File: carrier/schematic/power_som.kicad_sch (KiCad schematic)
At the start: 17 parts, among them U22004 TPS54302DDCR

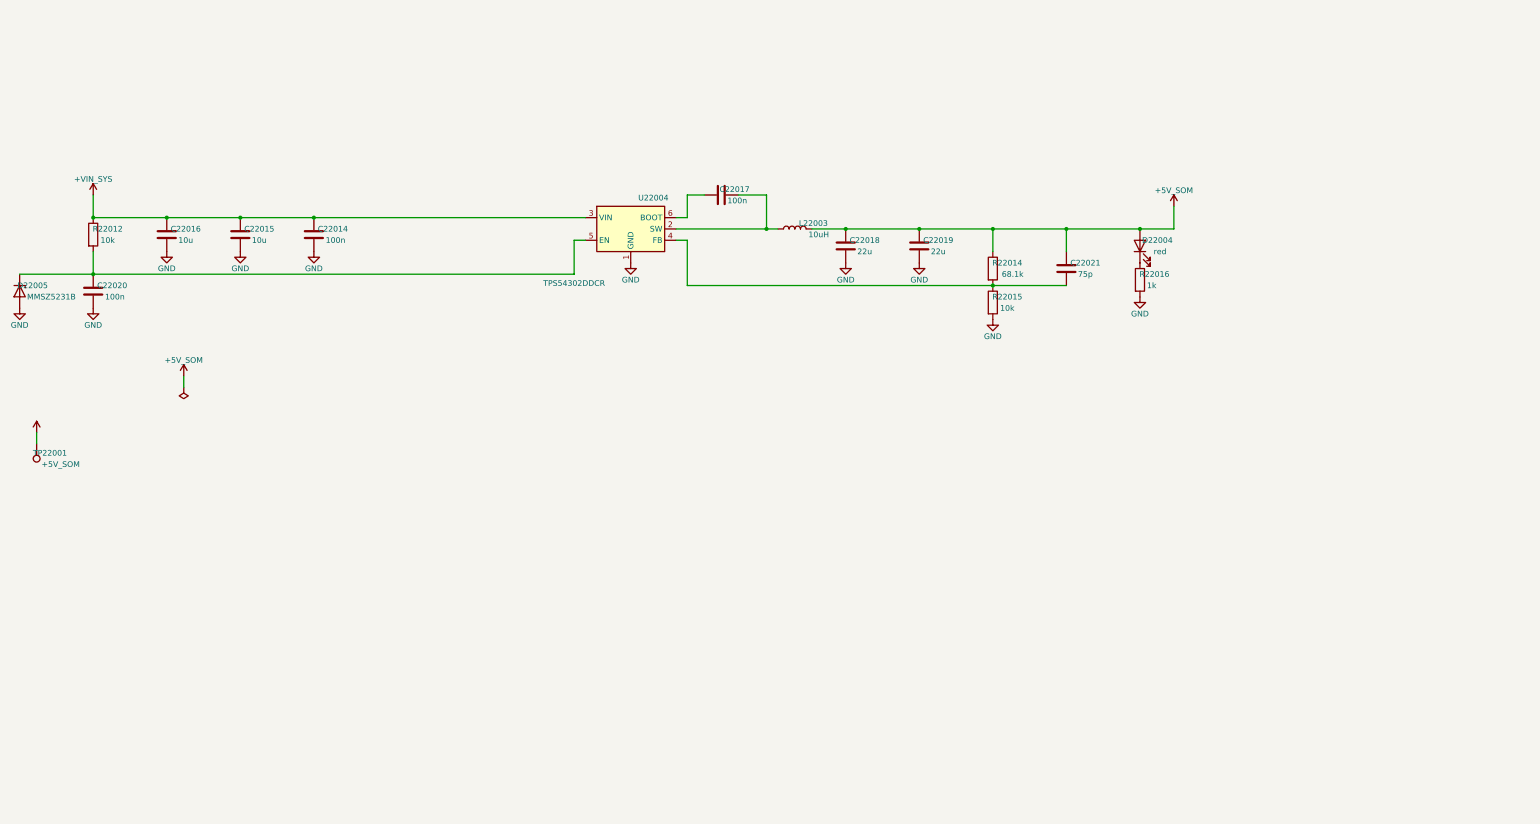
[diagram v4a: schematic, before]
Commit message: power: U2(+3V3)/U4(+5V_SOM) -> LM61460 EP buck (thermal HIGH fix) + honest thermal gate + LM61460 ratings + cleanup
Audit HIGH (re-verified vs TI SLVSDG6C): U2(+3V3 @2.745A) + U4(+5V_SOM @2.0A)
were TPS54302 SOT-23-6 NO-EP bucks; at the datasheet RθJA (118.9 JESD51-7 /
57.2 EVM) + Tj rec-max 125C, both ran OVER 125C even at the EVM best case
(U2 141C, U4 144C), and +3V3 sat at 92% of the 3A rating. The thermal gate hid
it with a fabricated RθJA=70.6 + a 140C guard.

- subsystems/power/power.py: U2 + U4 swapped to LM61460AANRJRR (the EP-equivalent
  6A buck already used for U1; PGND/SW pads->GND pour = heat path). Re-derived FB
  (Vref 1.0V): U2 22.1k/10k -> 3.21V; U4 47.5k/13k -> 4.654V (in the SoM 4.2-5.0V
  window); U4 EN-clamp (zener) preserved. power.cir + test_power updated.
  -> THERMAL PASS: U2 Tj 98C, U4 99C (was 141/144); 6A part at 46%/33% load.
- schgen/verify/thermal.py: HONEST re-base (LAW 4) — TPS54302 RθJA 70.6->118.9,
  tj_max 150->125 (rec-op, not abs); no-EP gets no pour credit; +test_thermal_gate
  (spec lock, >2A no-EP fails, EP passes).
- ratings.py: LM61460 C2864505 row (vin_max 42, i_max 6) — part_rules IC_VIN now
  covered; power_som docstring corrected; orphan parts/LMR33630ADDAR removed
  (MPQ4423 KEPT — live test fixture); spice/testpoints/firmware-README updated.
- schgen/layout/place.py: engine extended (box-buck EN-strap islet, both-dir
  left-pin escape, inter-stage + multi-rail-farm gaps for 2+ box-bucks) so the
  two-LM61460 power sheet places clean on A3 — every OTHER sheet byte-identical.

Verify: THERMAL/POWER TREE/PART RULES/SPICE/RATSNEST(LAW5) PASS; golden 33 match
(only power + power_som re-blessed, eyeballed clean); selftest 63/63; power suite
32 passed. __main__ + selftest untouched.

Co-Authored-By: Claude Opus 4.8 <noreply@anthropic.com>
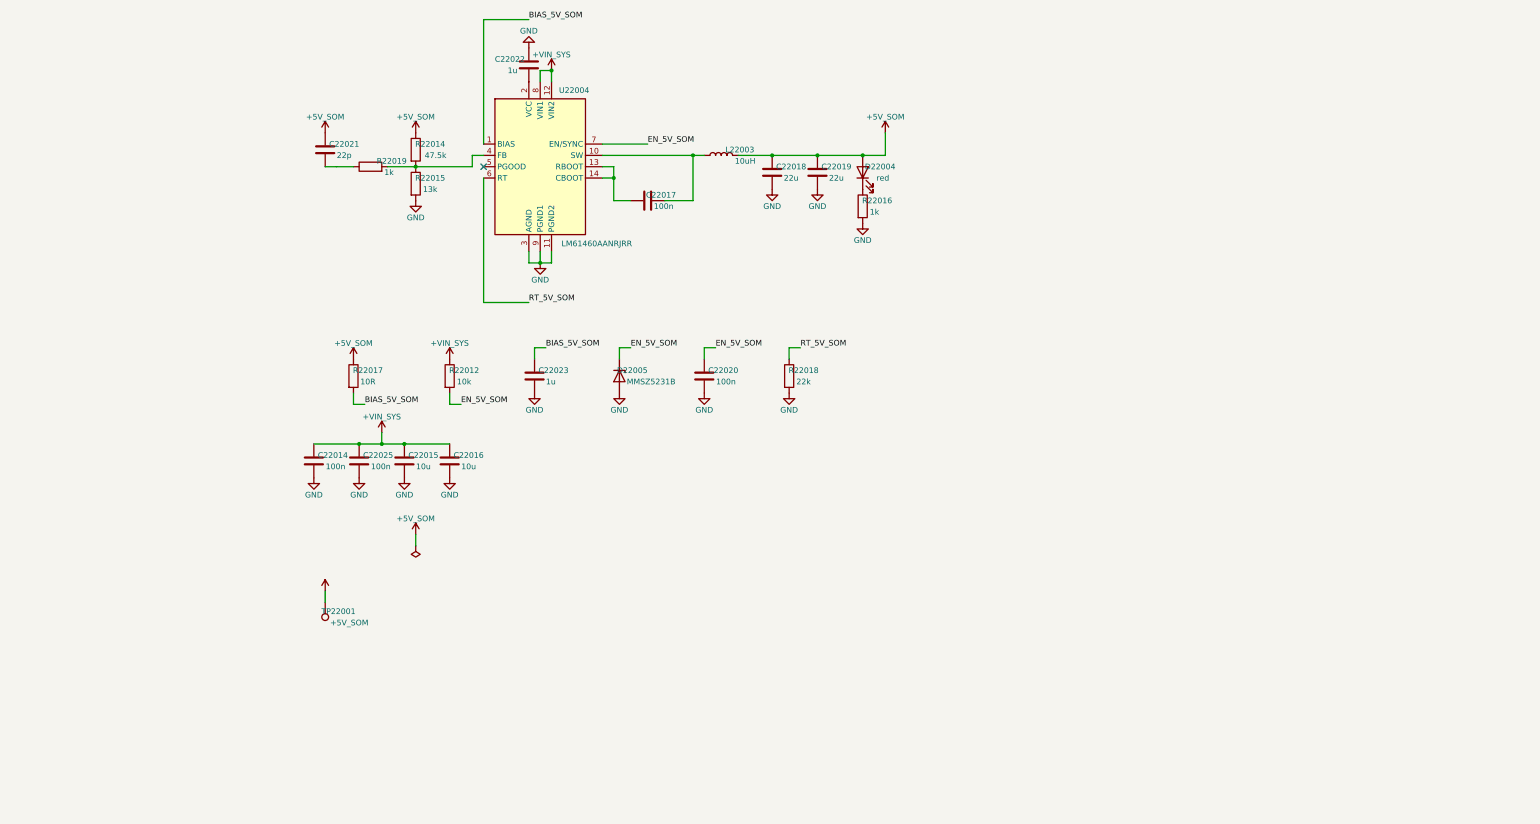
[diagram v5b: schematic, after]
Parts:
- added C22014, C22025: 100n, Capacitor_SMD:C_0603_1608Metric, symbol Device:C
- added C22015, C22016: 10u, Capacitor_SMD:C_1206_3216Metric, symbol Device:C
- added R22018: 22k, Resistor_SMD:R_0603_1608Metric, symbol Device:R
- added TP22001: +5V_SOM, TestPoint:TestPoint_Pad_D1.5mm, symbol Connector:TestPoint
- C22017: renamed from C22015; value 10u -> 100n; footprint Capacitor_SMD:C_1206_3216Metric -> Capacitor_SMD:C_0603_1608Metric; LCSC C13585 -> C14663
- C22018: renamed from R22012; value 10k -> 22u; footprint Resistor_SMD:R_0603_1608Metric -> Capacitor_SMD:C_0805_2012Metric; symbol Device:R -> Device:C; LCSC C25804 -> C45783
- C22019: renamed from C22020; value 100n -> 22u; footprint Capacitor_SMD:C_0603_1608Metric -> Capacitor_SMD:C_0805_2012Metric; LCSC C14663 -> C45783
- C22020: renamed from TP22001; value +5V_SOM -> 100n; footprint TestPoint:TestPoint_Pad_D1.5mm -> Capacitor_SMD:C_0603_1608Metric; symbol Connector:TestPoint -> Device:C; BOM exclude -> (none); LCSC (none) -> C14663
- C22021: renamed from C22018; value 22u -> 22p; footprint Capacitor_SMD:C_0805_2012Metric -> Capacitor_SMD:C_0603_1608Metric; LCSC C45783 -> C1653
- C22022: renamed from C22014; value 100n -> 1u; LCSC C14663 -> C15849
- C22023: renamed from D22004; value red -> 1u; footprint LED_SMD:LED_0603_1608Metric -> Capacitor_SMD:C_0603_1608Metric; symbol Device:LED -> Device:C; LCSC C2286 -> C15849
- D22004: renamed from C22019; value 22u -> red; footprint Capacitor_SMD:C_0805_2012Metric -> LED_SMD:LED_0603_1608Metric; symbol Device:C -> Device:LED; LCSC C45783 -> C2286
- D22005: renamed from R22016; value 1k -> MMSZ5231B; footprint Resistor_SMD:R_0603_1608Metric -> Diode_SMD:D_SOD-123; symbol Device:R -> Device:D_Zener; LCSC C21190 -> C85181
- L22003: renamed from C22016; value 10u -> 10uH; footprint Capacitor_SMD:C_1206_3216Metric -> SWPA8040S100MT:SWPA8040S100MT; symbol Device:C -> Device:L; LCSC C13585 -> C37429
- R22012: renamed from C22021; value 75p -> 10k; footprint Capacitor_SMD:C_0603_1608Metric -> Resistor_SMD:R_0603_1608Metric; symbol Device:C -> Device:R; LCSC C22399620 -> C25804
- R22014: renamed from D22005; value MMSZ5231B -> 47.5k; footprint Diode_SMD:D_SOD-123 -> Resistor_SMD:R_0603_1608Metric; symbol Device:D_Zener -> Device:R; LCSC C85181 -> C23061
- R22015: renamed from C22017; value 100n -> 13k; footprint Capacitor_SMD:C_0603_1608Metric -> Resistor_SMD:R_0603_1608Metric; symbol Device:C -> Device:R; LCSC C14663 -> C22797
- R22016: renamed from R22014; value 68.1k -> 1k; LCSC C844583 -> C21190
- R22017: renamed from R22015; value 10k -> 10R; LCSC C25804 -> C22859
- R22019: renamed from L22003; value 10uH -> 1k; footprint SWPA8040S100MT:SWPA8040S100MT -> Resistor_SMD:R_0603_1608Metric; symbol Device:L -> Device:R; LCSC C37429 -> C21190
- U22004: value TPS54302DDCR -> LM61460AANRJRR; footprint Package_TO_SOT_SMD:TSOT-23-6 -> LM61460AANRJRR:LM61460AANRJRR; symbol Regulator_Switching:TPS54302 -> LM61460AANRJRR:LM61460AANRJRR; LCSC C311983 -> C2864505; MPN TPS54302DDCR -> (none)
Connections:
- net +5V_SOM: now also C22018.1, C22019.1, D22004.2 (A), L22003.2, R22014.1, R22017.1, TP22001.1; no longer C22020.1, C22023.2 (A), D22004.1, R22012.1, R22016.1, R22019.2
- net +VIN_SYS: now also R22012.1, U22004.12 (VIN2), U22004.8 (VIN1), C22014.1, C22015.1, C22016.1, C22025.1; no longer C22017.1, C22018.1, C22022.1, L22003.1, U22004.3 (VIN)
- net GND: now also C22018.2, C22020.2, C22023.2, R22015.2, R22016.2, U22004.11 (PGND2), U22004.3 (AGND), U22004.9 (PGND1), C22014.2, C22015.2, C22016.2, C22025.2, R22018.2; no longer C22017.2, C22021.2, D22004.2, L22003.2, R22014.2 (A), R22017.2, U22004.1 (GND)
- net at R22015.1: now also R22014.2, R22019.2, U22004.4 (FB); no longer U22004.6 (BOOT)
- net BIAS_5V_SOM: now reaches C22023.1
- net BIAS_5V_SOM: now also R22017.2, U22004.1 (BIAS); no longer D22005.1
- new net: D22004.1 (K), R22016.1
- new net: C22017.2, L22003.1, U22004.10 (SW)
- new net: C22017.1, U22004.13 (RBOOT), U22004.14 (CBOOT)
- new net: C22022.1, U22004.2 (VCC)
- new net: C22021.2, R22019.1
- new net EN_5V_SOM: C22020.1, D22005.1 (K), R22012.2, U22004.7 (EN/SYNC)
- new net RT_5V_SOM: R22018.1, U22004.6 (RT)
- now unconnected: U22004.5 (EN)
- no-connect marks 0 -> 1
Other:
- moved on the sheet: C22017, C22019, C22021, C22022, R22016, R22017

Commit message: fix(silk): tighten 6 sheet titles overflowing the title-block cell (M6)
The audit flagged 6 sheet titles whose text overflowed the KiCad title-block
Title cell, crossing the border/zone rules (LAW 1). Root cause: the authored
Circuit titles were longer than the cell renders (the fit boundary is ~58 chars
of typical text; these were 55-73). Tightened all 6 at the source (display-only
strings, no info-loss of the essentials, cannot affect netlist/routing — board
.kicad_pcb byte-unchanged):
- board_services 73->47, pmod_expansion 65->45, mechanical 60->50,
  usb_jtag 59->38, usb_jtag_connector 58->42, power_som 55->37.
Render-confirmed: board_services + mechanical (the longest) now end well inside
the cell. The gallery description table (carrier/README.md) regenerated to match.
666 tests pass at HEAD; the 3 title-asserting tests (som_j1/j2/j3) are untouched.

Co-Authored-By: Claude Opus 4.8 <noreply@anthropic.com>
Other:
- title: Power: +VIN -> +5V_SOM always-on buck (SoM VIN, P0 fix) -> Power: +VIN -> +5V_SOM always-on buck
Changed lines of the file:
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@@
 	(paper "A4")
 	(title_block
-		(title "Power: +VIN -> +5V_SOM always-on buck (SoM VIN, P0 fix)")
+		(title "Power: +VIN -> +5V_SOM always-on buck")
 		(company "Zynq SoM Carrier")
 		(comment 1 "power_som — generated by schgen (do not hand-edit)")
